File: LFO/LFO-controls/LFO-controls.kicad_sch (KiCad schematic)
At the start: 21 parts, among them J10 Conn_01x06, J11 Conn_01x01, J12 Conn_01x01, J13 Conn_01x01, J14 Conn_01x01, J15 Conn_01x03, J2 AudioJack2, J9 Conn_01x06

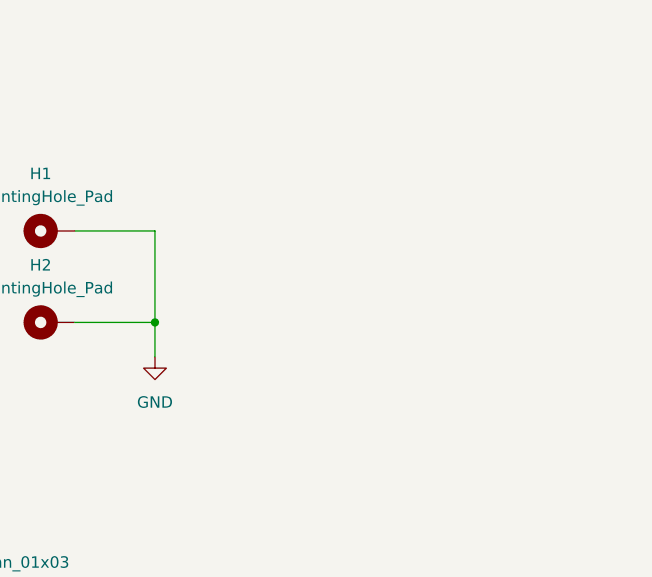
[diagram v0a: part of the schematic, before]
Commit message: LFO panel, not fully routed
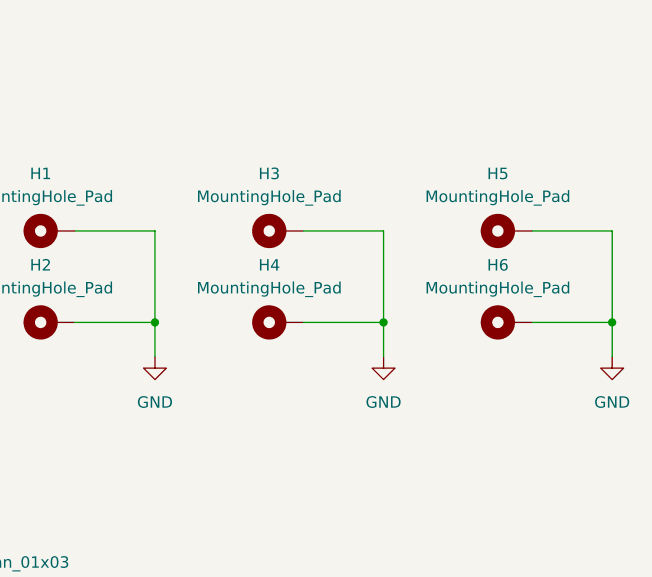
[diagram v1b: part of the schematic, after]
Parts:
- added H3, H4, H5, H6: MountingHole_Pad, MountingHole:MountingHole_3.2mm_M3_DIN965_Pad, symbol Mechanical:MountingHole_Pad
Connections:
- net GND: now also H3.1, H4.1, H5.1, H6.1
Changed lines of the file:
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@@
 (kicad_sch (version 20230121) (generator eeschema)
   (paper "A4")
+  (junction (at 245.11 83.82) (diameter 0) (color 0 0 0 0)
+  )
   (junction (at 194.31 83.82) (diameter 0) (color 0 0 0 0)
   )
+  (junction (at 219.71 83.82) (diameter 0) (color 0 0 0 0)
+  )
   (wire (pts (xy 92.71 53.34) (xy 95.25 53.34))
     (stroke (width 0) (type default))
@@
     (stroke (width 0) (type default))
   )
+  (wire (pts (xy 219.71 83.82) (xy 219.71 73.66))
+    (stroke (width 0) (type default))
+  )
   (wire (pts (xy 33.02 119.38) (xy 33.02 120.65))
     (stroke (width 0) (type default))
@@
     (stroke (width 0) (type default))
   )
+  (wire (pts (xy 245.11 83.82) (xy 245.11 87.63))
+    (stroke (width 0) (type default))
+  )
   (wire (pts (xy 36.83 54.61) (xy 39.37 54.61))
     (stroke (width 0) (type default))
@@
     (stroke (width 0) (type default))
   )
+  (wire (pts (xy 245.11 83.82) (xy 245.11 73.66))
+    (stroke (width 0) (type default))
+  )
   (wire (pts (xy 142.24 44.45) (xy 144.78 44.45))
     (stroke (width 0) (type default))
@@
     (stroke (width 0) (type default))
   )
+  (wire (pts (xy 245.11 73.66) (xy 236.22 73.66))
+    (stroke (width 0) (type default))
+  )
   (wire (pts (xy 166.37 106.68) (xy 163.83 106.68))
     (stroke (width 0) (type default))
@@
     (stroke (width 0) (type default))
   )
+  (wire (pts (xy 219.71 83.82) (xy 219.71 87.63))
+    (stroke (width 0) (type default))
+  )
   (wire (pts (xy 104.14 139.7) (xy 106.68 139.7))
     (stroke (width 0) (type default))
@@
     (stroke (width 0) (type default))
   )
+  (wire (pts (xy 219.71 73.66) (xy 210.82 73.66))
+    (stroke (width 0) (type default))
+  )
   (wire (pts (xy 54.61 116.84) (xy 57.15 116.84))
     (stroke (width 0) (type default))
@@
     (stroke (width 0) (type default))
   )
+  (wire (pts (xy 210.82 83.82) (xy 219.71 83.82))
+    (stroke (width 0) (type default))
+  )
   (wire (pts (xy 54.61 77.47) (xy 57.15 77.47))
     (stroke (width 0) (type default))
@@
   )
   (wire (pts (xy 54.61 105.41) (xy 55.88 105.41))
+    (stroke (width 0) (type default))
+  )
+  (wire (pts (xy 236.22 83.82) (xy 245.11 83.82))
     (stroke (width 0) (type default))
   )
@@
     )
   )
+  (symbol (lib_id "Mechanical:MountingHole_Pad") (at 233.68 83.82 90) (unit 1)
+    (in_bom yes) (on_board yes) (dnp no) (fields_autoplaced)
+    (property "Reference" "H6" (at 232.41 77.47 90)
+      (effects (font (size 1.27 1.27)))
+    )
+    (property "Value" "MountingHole_Pad" (at 232.41 80.01 90)
+      (effects (font (size 1.27 1.27)))
+    )
+    (property "Footprint" "MountingHole:MountingHole_3.2mm_M3_DIN965_Pad" (at 233.68 83.82 0)
+      (effects (font (size 1.27 1.27)) hide)
+    )
+    (property "Datasheet" "~" (at 233.68 83.82 0)
+      (effects (font (size 1.27 1.27)) hide)
+    )
+    (pin "1")
+    (instances
+      (project "LFO-controls"
+        (path "/938c5bc2-f32a-4a3a-8ab9-029566134c63"
+          (reference "H6") (unit 1)
+        )
+      )
+      (project "VCA"
+        (path "/a331be11-cf92-4101-a082-e20022c8dee2/105b1da3-69f9-4444-a8b7-56e3901da034"
+          (reference "H2") (unit 1)
+        )
+      )
+      (project "LFO"
+        (path "/acd84bd8-c29a-4e4d-a78d-bbb1d32e037c/764b8532-46b5-43ba-a119-e7e4e00258ed"
+          (reference "H2") (unit 1)
+        )
+      )
+    )
+  )
   (symbol (lib_id "Device:LED") (at 138.43 44.45 180) (unit 1)
     (in_bom yes) (on_board yes) (dnp no) (fields_autoplaced)
@@
         (path "/938c5bc2-f32a-4a3a-8ab9-029566134c63"
           (reference "#PWR05") (unit 1)
+        )
+      )
+    )
+  )
+  (symbol (lib_id "Mechanical:MountingHole_Pad") (at 208.28 83.82 90) (unit 1)
+    (in_bom yes) (on_board yes) (dnp no) (fields_autoplaced)
+    (property "Reference" "H4" (at 207.01 77.47 90)
+      (effects (font (size 1.27 1.27)))
+    )
+    (property "Value" "MountingHole_Pad" (at 207.01 80.01 90)
+      (effects (font (size 1.27 1.27)))
+    )
+    (property "Footprint" "MountingHole:MountingHole_3.2mm_M3_DIN965_Pad" (at 208.28 83.82 0)
+      (effects (font (size 1.27 1.27)) hide)
+    )
+    (property "Datasheet" "~" (at 208.28 83.82 0)
+      (effects (font (size 1.27 1.27)) hide)
+    )
+    (pin "1")
+    (instances
+      (project "LFO-controls"
+        (path "/938c5bc2-f32a-4a3a-8ab9-029566134c63"
+          (reference "H4") (unit 1)
+        )
+      )
+      (project "VCA"
+        (path "/a331be11-cf92-4101-a082-e20022c8dee2/105b1da3-69f9-4444-a8b7-56e3901da034"
+          (reference "H2") (unit 1)
+        )
+      )
+      (project "LFO"
+        (path "/acd84bd8-c29a-4e4d-a78d-bbb1d32e037c/764b8532-46b5-43ba-a119-e7e4e00258ed"
+          (reference "H2") (unit 1)
         )
       )
@@
     )
   )
+  (symbol (lib_id "Mechanical:MountingHole_Pad") (at 233.68 73.66 90) (unit 1)
+    (in_bom yes) (on_board yes) (dnp no) (fields_autoplaced)
+    (property "Reference" "H5" (at 232.41 67.31 90)
+      (effects (font (size 1.27 1.27)))
+    )
+    (property "Value" "MountingHole_Pad" (at 232.41 69.85 90)
+      (effects (font (size 1.27 1.27)))
+    )
+    (property "Footprint" "MountingHole:MountingHole_3.2mm_M3_DIN965_Pad" (at 233.68 73.66 0)
+      (effects (font (size 1.27 1.27)) hide)
+    )
+    (property "Datasheet" "~" (at 233.68 73.66 0)
+      (effects (font (size 1.27 1.27)) hide)
+    )
+    (pin "1")
+    (instances
+      (project "LFO-controls"
+        (path "/938c5bc2-f32a-4a3a-8ab9-029566134c63"
+          (reference "H5") (unit 1)
+        )
+      )
+      (project "VCA"
+        (path "/a331be11-cf92-4101-a082-e20022c8dee2/105b1da3-69f9-4444-a8b7-56e3901da034"
+          (reference "H1") (unit 1)
+        )
+      )
+      (project "LFO"
+        (path "/acd84bd8-c29a-4e4d-a78d-bbb1d32e037c/764b8532-46b5-43ba-a119-e7e4e00258ed"
+          (reference "H1") (unit 1)
+        )
+      )
+    )
+  )
   (symbol (lib_id "Mechanical:MountingHole_Pad") (at 182.88 83.82 90) (unit 1)
     (in_bom yes) (on_board yes) (dnp no) (fields_autoplaced)
@@
         )
       )
+    )
+  )
+  (symbol (lib_id "power:GND") (at 245.11 87.63 0) (unit 1)
+    (in_bom yes) (on_board yes) (dnp no) (fields_autoplaced)
+    (property "Reference" "#PWR017" (at 245.11 93.98 0)
+      (effects (font (size 1.27 1.27)) hide)
+    )
+    (property "Value" "GND" (at 245.11 92.71 0)
+      (effects (font (size 1.27 1.27)))
+    )
+    (property "Footprint" "" (at 245.11 87.63 0)
+      (effects (font (size 1.27 1.27)) hide)
+    )
+    (property "Datasheet" "" (at 245.11 87.63 0)
+      (effects (font (size 1.27 1.27)) hide)
+    )
+    (pin "1")
+    (instances
+      (project "LFO-controls"
+        (path "/938c5bc2-f32a-4a3a-8ab9-029566134c63"
+          (reference "#PWR017") (unit 1)
+        )
+      )
+      (project "VCA"
+        (path "/a331be11-cf92-4101-a082-e20022c8dee2/105b1da3-69f9-4444-a8b7-56e3901da034"
+          (reference "#PWR061") (unit 1)
+        )
+      )
+      (project "LFO"
+        (path "/acd84bd8-c29a-4e4d-a78d-bbb1d32e037c/764b8532-46b5-43ba-a119-e7e4e00258ed"
+          (reference "#PWR057") (unit 1)
+        )
+      )
+    )
+  )
+  (symbol (lib_id "power:GND") (at 219.71 87.63 0) (unit 1)
+    (in_bom yes) (on_board yes) (dnp no) (fields_autoplaced)
+    (property "Reference" "#PWR016" (at 219.71 93.98 0)
+      (effects (font (size 1.27 1.27)) hide)
+    )
+    (property "Value" "GND" (at 219.71 92.71 0)
+      (effects (font (size 1.27 1.27)))
+    )
+    (property "Footprint" "" (at 219.71 87.63 0)
+      (effects (font (size 1.27 1.27)) hide)
+    )
+    (property "Datasheet" "" (at 219.71 87.63 0)
+      (effects (font (size 1.27 1.27)) hide)
+    )
+    (pin "1")
+    (instances
+      (project "LFO-controls"
+        (path "/938c5bc2-f32a-4a3a-8ab9-029566134c63"
+          (reference "#PWR016") (unit 1)
+        )
+      )
+      (project "VCA"
+        (path "/a331be11-cf92-4101-a082-e20022c8dee2/105b1da3-69f9-4444-a8b7-56e3901da034"
+          (reference "#PWR061") (unit 1)
+        )
+      )
+      (project "LFO"
+        (path "/acd84bd8-c29a-4e4d-a78d-bbb1d32e037c/764b8532-46b5-43ba-a119-e7e4e00258ed"
+          (reference "#PWR057") (unit 1)
+        )
+      )
+    )
+  )
+  (symbol (lib_id "Mechanical:MountingHole_Pad") (at 208.28 73.66 90) (unit 1)
+    (in_bom yes) (on_board yes) (dnp no) (fields_autoplaced)
+    (property "Reference" "H3" (at 207.01 67.31 90)
+      (effects (font (size 1.27 1.27)))
+    )
+    (property "Value" "MountingHole_Pad" (at 207.01 69.85 90)
+      (effects (font (size 1.27 1.27)))
+    )
+    (property "Footprint" "MountingHole:MountingHole_3.2mm_M3_DIN965_Pad" (at 208.28 73.66 0)
+      (effects (font (size 1.27 1.27)) hide)
+    )
+    (property "Datasheet" "~" (at 208.28 73.66 0)
+      (effects (font (size 1.27 1.27)) hide)
+    )
+    (pin "1")
+    (instances
+      (project "LFO-controls"
+        (path "/938c5bc2-f32a-4a3a-8ab9-029566134c63"
+          (reference "H3") (unit 1)
+        )
+      )
+      (project "VCA"
+        (path "/a331be11-cf92-4101-a082-e20022c8dee2/105b1da3-69f9-4444-a8b7-56e3901da034"
+          (reference "H1") (unit 1)
+        )
+      )
+      (project "LFO"
+        (path "/acd84bd8-c29a-4e4d-a78d-bbb1d32e037c/764b8532-46b5-43ba-a119-e7e4e00258ed"
+          (reference "H1") (unit 1)
+        )
+      )

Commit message: minor fixes after first build
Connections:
- net CFH: now also RV2.1; no longer RV2.3
- net CFL: now also RV2.3; no longer RV2.1
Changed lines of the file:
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@@
+    (stroke (width 0) (type default))
+  )
+  (wire (pts (xy 104.14 121.92) (xy 106.68 121.92))
+    (stroke (width 0) (type default))
+  )
+  (wire (pts (xy 104.14 119.38) (xy 106.68 119.38))
+    (stroke (width 0) (type default))
+  )
+  (wire (pts (xy 34.29 80.01) (xy 34.29 82.55))
+    (stroke (width 0) (type default))
+  )
+  (wire (pts (xy 107.95 80.01) (xy 110.49 80.01))
+    (stroke (width 0) (type default))
+  )
+  (wire (pts (xy 31.75 116.84) (xy 34.29 116.84))
+    (stroke (width 0) (type default))
+  )
+  (wire (pts (xy 219.71 83.82) (xy 219.71 73.66))
     (stroke (width 0) (type default))
   )
@@
     (stroke (width 0) (type default))
   )
-  (wire (pts (xy 104.14 121.92) (xy 106.68 121.92))
-    (stroke (width 0) (type default))
-  )
-  (wire (pts (xy 104.14 119.38) (xy 106.68 119.38))
-    (stroke (width 0) (type default))
-  )
-  (wire (pts (xy 34.29 80.01) (xy 34.29 82.55))
-    (stroke (width 0) (type default))
-  )
-  (wire (pts (xy 107.95 80.01) (xy 110.49 80.01))
-    (stroke (width 0) (type default))
-  )
-  (wire (pts (xy 31.75 116.84) (xy 34.29 116.84))
-    (stroke (width 0) (type default))
-  )
-  (wire (pts (xy 219.71 83.82) (xy 219.71 73.66))
-    (stroke (width 0) (type default))
-  )
   (wire (pts (xy 33.02 119.38) (xy 33.02 120.65))
     (stroke (width 0) (type default))
@@
     (stroke (width 0) (type default))
   )
+  (wire (pts (xy 58.42 57.15) (xy 58.42 59.69))
+    (stroke (width 0) (type default))
+  )
   (wire (pts (xy 31.75 119.38) (xy 33.02 119.38))
     (stroke (width 0) (type default))
@@
   )
   (wire (pts (xy 166.37 109.22) (xy 158.75 109.22))
-    (stroke (width 0) (type default))
-  )
-  (wire (pts (xy 58.42 57.15) (xy 58.42 59.69))
     (stroke (width 0) (type default))
   )
@@
   (symbol (lib_id "power:GND") (at 34.29 106.68 0) (unit 1)
     (in_bom yes) (on_board yes) (dnp no) (fields_autoplaced)
-    (property "Reference" "#PWR03" (at 34.29 113.03 0)
+    (property "Reference" "#PWR06" (at 34.29 113.03 0)
       (effects (font (size 1.27 1.27)) hide)
     )
@@
       (project "LFO-controls"
         (path "/938c5bc2-f32a-4a3a-8ab9-029566134c63"
-          (reference "#PWR03") (unit 1)
+          (reference "#PWR06") (unit 1)
         )
       )
@@
   (symbol (lib_id "power:-12V") (at 33.02 59.69 180) (unit 1)
     (in_bom yes) (on_board yes) (dnp no) (fields_autoplaced)
-    (property "Reference" "#PWR09" (at 33.02 62.23 0)
+    (property "Reference" "#PWR02" (at 33.02 62.23 0)
       (effects (font (size 1.27 1.27)) hide)
     )
@@
       (project "LFO-controls"
         (path "/938c5bc2-f32a-4a3a-8ab9-029566134c63"
-          (reference "#PWR09") (unit 1)
+          (reference "#PWR02") (unit 1)
         )
       )
@@
       (project "LFO-controls"
         (path "/938c5bc2-f32a-4a3a-8ab9-029566134c63"
-          (reference "RV1") (unit 1)
+          (reference "FINE1") (unit 1)
         )
       )
@@
       (project "LFO-controls"
         (path "/938c5bc2-f32a-4a3a-8ab9-029566134c63"
-          (reference "J8") (unit 1)
+          (reference "J7") (unit 1)
         )
       )
@@
       (project "LFO-controls"
         (path "/938c5bc2-f32a-4a3a-8ab9-029566134c63"
-          (reference "J3") (unit 1)
+          (reference "J2") (unit 1)
         )
       )
@@
       (project "LFO-controls"
         (path "/938c5bc2-f32a-4a3a-8ab9-029566134c63"
-          (reference "J5") (unit 1)
+          (reference "J4") (unit 1)
         )
       )
@@
   (symbol (lib_id "power:GND") (at 33.02 120.65 0) (unit 1)
     (in_bom yes) (on_board yes) (dnp no) (fields_autoplaced)
-    (property "Reference" "#PWR04" (at 33.02 127 0)
+    (property "Reference" "#PWR03" (at 33.02 127 0)
       (effects (font (size 1.27 1.27)) hide)
     )
@@
       (project "LFO-controls"
         (path "/938c5bc2-f32a-4a3a-8ab9-029566134c63"
-          (reference "#PWR04") (unit 1)
+          (reference "#PWR03") (unit 1)
         )
       )
@@
   (symbol (lib_id "power:+12V") (at 33.02 48.26 0) (unit 1)
     (in_bom yes) (on_board yes) (dnp no) (fields_autoplaced)
-    (property "Reference" "#PWR010" (at 33.02 52.07 0)
+    (property "Reference" "#PWR01" (at 33.02 52.07 0)
       (effects (font (size 1.27 1.27)) hide)
     )
@@
       (project "LFO-controls"
         (path "/938c5bc2-f32a-4a3a-8ab9-029566134c63"
-          (reference "#PWR010") (unit 1)
+          (reference "#PWR01") (unit 1)
         )
       )
@@
       (project "LFO-controls"
         (path "/938c5bc2-f32a-4a3a-8ab9-029566134c63"
-          (reference "RV3") (unit 1)
+          (reference "PW1") (unit 1)
         )
       )
@@
       (project "LFO-controls"
         (path "/938c5bc2-f32a-4a3a-8ab9-029566134c63"
-          (reference "J1") (unit 1)
+          (reference "J8") (unit 1)
         )
       )
@@
       (project "LFO-controls"
         (path "/938c5bc2-f32a-4a3a-8ab9-029566134c63"
-          (reference "J4") (unit 1)
+          (reference "J3") (unit 1)
         )
       )
@@
   (symbol (lib_id "power:GND") (at 34.29 95.25 0) (unit 1)
     (in_bom yes) (on_board yes) (dnp no) (fields_autoplaced)
-    (property "Reference" "#PWR02" (at 34.29 101.6 0)
+    (property "Reference" "#PWR05" (at 34.29 101.6 0)
       (effects (font (size 1.27 1.27)) hide)
     )
@@
       (project "LFO-controls"
         (path "/938c5bc2-f32a-4a3a-8ab9-029566134c63"
-          (reference "#PWR02") (unit 1)
+          (reference "#PWR05") (unit 1)
         )
       )
@@
   (symbol (lib_id "power:GND") (at 57.15 120.65 0) (unit 1)
     (in_bom yes) (on_board yes) (dnp no) (fields_autoplaced)
-    (property "Reference" "#PWR05" (at 57.15 127 0)
+    (property "Reference" "#PWR010" (at 57.15 127 0)
       (effects (font (size 1.27 1.27)) hide)
     )
@@
       (project "LFO-controls"
         (path "/938c5bc2-f32a-4a3a-8ab9-029566134c63"
-          (reference "#PWR05") (unit 1)
+          (reference "#PWR010") (unit 1)
         )
       )
@@
       (project "LFO-controls"
         (path "/938c5bc2-f32a-4a3a-8ab9-029566134c63"
-          (reference "J7") (unit 1)
+          (reference "J6") (unit 1)
         )
       )
@@
       (project "LFO-controls"
         (path "/938c5bc2-f32a-4a3a-8ab9-029566134c63"
-          (reference "J2") (unit 1)
+          (reference "J1") (unit 1)
         )
       )
@@
   (symbol (lib_id "power:GND") (at 55.88 106.68 0) (unit 1)
     (in_bom yes) (on_board yes) (dnp no) (fields_autoplaced)
-    (property "Reference" "#PWR06" (at 55.88 113.03 0)
+    (property "Reference" "#PWR08" (at 55.88 113.03 0)
       (effects (font (size 1.27 1.27)) hide)
     )
@@
       (project "LFO-controls"
         (path "/938c5bc2-f32a-4a3a-8ab9-029566134c63"
-          (reference "#PWR06") (unit 1)
+          (reference "#PWR08") (unit 1)
         )
       )
@@
       (project "LFO-controls"
         (path "/938c5bc2-f32a-4a3a-8ab9-029566134c63"
-          (reference "J6") (unit 1)
+          (reference "J5") (unit 1)
         )
       )
@@
       (project "LFO-controls"
         (path "/938c5bc2-f32a-4a3a-8ab9-029566134c63"
-          (reference "#PWR015") (unit 1)
+          (reference "#PWR011") (unit 1)
         )
       )
@@
   (symbol (lib_id "power:GND") (at 34.29 82.55 0) (unit 1)
     (in_bom yes) (on_board yes) (dnp no) (fields_autoplaced)
-    (property "Reference" "#PWR01" (at 34.29 88.9 0)
+    (property "Reference" "#PWR04" (at 34.29 88.9 0)
       (effects (font (size 1.27 1.27)) hide)
     )
@@
       (project "LFO-controls"
         (path "/938c5bc2-f32a-4a3a-8ab9-029566134c63"
-          (reference "#PWR01") (unit 1)
-        )
-      )
-    )
-  )
-  (symbol (lib_id "Device:R_Potentiometer") (at 58.42 53.34 0) (mirror x) (unit 1)
+          (reference "#PWR04") (unit 1)
+        )
+      )
+    )
+  )
+  (symbol (lib_id "Device:R_Potentiometer") (at 58.42 53.34 0) (unit 1)
     (in_bom yes) (on_board yes) (dnp no)
-    (property "Reference" "RV2" (at 55.88 54.61 0)
+    (property "Reference" "RV2" (at 55.88 52.07 0)
       (effects (font (size 1.27 1.27)) (justify right))
     )
-    (property "Value" "R_Potentiometer" (at 55.88 52.07 0)
+    (property "Value" "R_Potentiometer" (at 55.88 54.61 0)
       (effects (font (size 1.27 1.27)) (justify right))
     )
@@
       (project "LFO-controls"
         (path "/938c5bc2-f32a-4a3a-8ab9-029566134c63"
-          (reference "RV2") (unit 1)
+          (reference "COARSE1") (unit 1)
         )
       )
@@
   (symbol (lib_id "power:GND") (at 55.88 81.28 0) (unit 1)
     (in_bom yes) (on_board yes) (dnp no) (fields_autoplaced)
-    (property "Reference" "#PWR08" (at 55.88 87.63 0)
+    (property "Reference" "#PWR07" (at 55.88 87.63 0)
       (effects (font (size 1.27 1.27)) hide)
     )
@@
       (project "LFO-controls"
         (path "/938c5bc2-f32a-4a3a-8ab9-029566134c63"
-          (reference "#PWR08") (unit 1)
+          (reference "#PWR07") (unit 1)
         )
       )
@@
   (symbol (lib_id "power:GND") (at 57.15 93.98 0) (unit 1)
     (in_bom yes) (on_board yes) (dnp no) (fields_autoplaced)
-    (property "Reference" "#PWR07" (at 57.15 100.33 0)
+    (property "Reference" "#PWR09" (at 57.15 100.33 0)
       (effects (font (size 1.27 1.27)) hide)
     )
@@
       (project "LFO-controls"
         (path "/938c5bc2-f32a-4a3a-8ab9-029566134c63"
-          (reference "#PWR07") (unit 1)
+          (reference "#PWR09") (unit 1)
         )
       )
@@
   (symbol (lib_id "power:GND") (at 194.31 87.63 0) (unit 1)
     (in_bom yes) (on_board yes) (dnp no) (fields_autoplaced)
-    (property "Reference" "#PWR011" (at 194.31 93.98 0)
+    (property "Reference" "#PWR015" (at 194.31 93.98 0)
       (effects (font (size 1.27 1.27)) hide)
     )
@@
       (project "LFO-controls"
         (path "/938c5bc2-f32a-4a3a-8ab9-029566134c63"
-          (reference "#PWR011") (unit 1)
-        )
-      )
+          (reference "#PWR015") (unit 1)
+        )
+      )
